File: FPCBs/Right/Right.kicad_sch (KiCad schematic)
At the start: 25 parts, among them J1 PCB, J2 LEDs, J3 LEDs, J4 shutter+1st_dial, J5 2nd Focus+Shutter, J6 Conn_01x03_Pin, SW1 Mode Dial, SW2 ON/OFF, SW3 Focus+Shutter, SW4 Focus+Shutter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

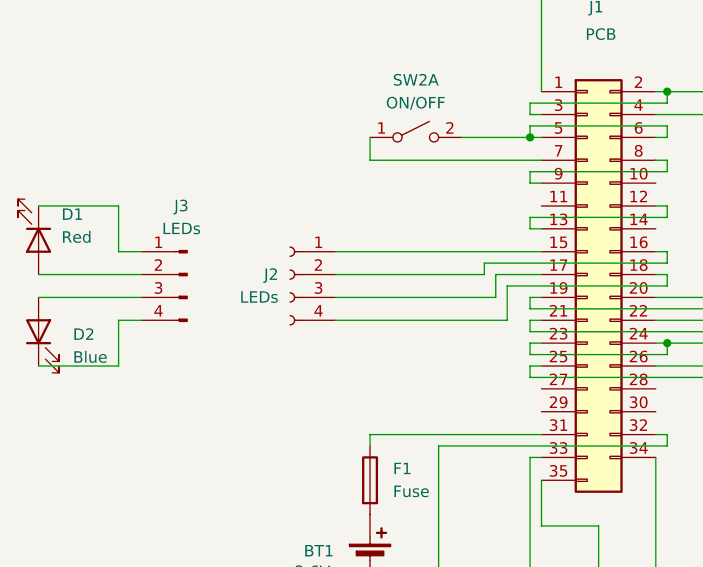
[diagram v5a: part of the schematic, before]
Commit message: Move leds to Right board
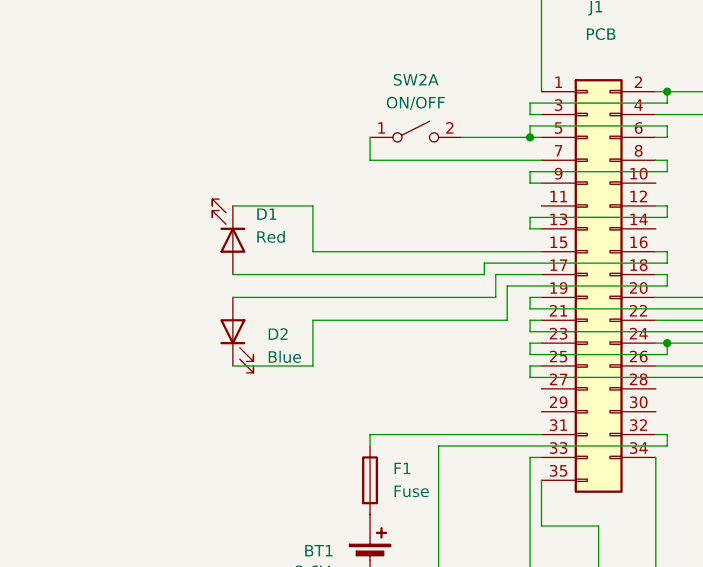
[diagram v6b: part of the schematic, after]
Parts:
- removed J2: LEDs, Leica-G9ii:Connector-4Pins, symbol Connector:Conn_01x04_Socket
- removed J3: LEDs, Leica-G9ii:Connector-4Pins, symbol Connector:Conn_01x04_Pin
- D1, D2: footprint LED_SMD:LED_0402_1005Metric -> Leica-G9ii:LED
- F1: footprint Fuse:Fuse_0402_1005Metric -> Leica-G9ii:R_2x1mm
- R1, R2, R3, R4, R5, R6, R7, R8: footprint Resistor_SMD:R_0201_0603Metric -> Leica-G9ii:R_2x1mm
- SW2: footprint Leica-G9ii:Switch_Power -> Leica-G9ii:Switch_Detection_Bidirectional
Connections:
- net at J1.15 (Pin_15): now also D1.1 (K)
- net at J1.16 (Pin_16): now also D1.2 (A)
- net at J1.17 (Pin_17): now also D2.2 (A)
- net at J1.18 (Pin_18): now also D2.1 (K)
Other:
- moved on the sheet: D1, D2
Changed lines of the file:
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@@
 	(wire
 		(pts
-			(xy 24.13 80.01) (xy 35.56 80.01)
+			(xy 45.72 80.01) (xy 74.93 80.01)
 		)
 		(stroke
@@
 	(wire
 		(pts
-			(xy 33.02 82.55) (xy 35.56 82.55)
+			(xy 54.61 82.55) (xy 76.2 82.55)
 		)
 		(stroke
@@
 	(wire
 		(pts
-			(xy 57.15 74.93) (xy 80.01 74.93)
-		)
-		(stroke
-			(width 0)
-			(type default)
-		)
-	)
-	(wire
-		(pts
 			(xy 74.93 80.01) (xy 74.93 77.47)
 		)
@@
 	(wire
 		(pts
-			(xy 57.15 82.55) (xy 76.2 82.55)
-		)
-		(stroke
-			(width 0)
-			(type default)
-		)
-	)
-	(wire
-		(pts
 			(xy 153.67 127) (xy 153.67 139.7)
 		)
@@
 	(wire
 		(pts
-			(xy 57.15 80.01) (xy 74.93 80.01)
-		)
-		(stroke
-			(width 0)
-			(type default)
-		)
-	)
-	(wire
-		(pts
 			(xy 78.74 86.36) (xy 78.74 85.09)
 		)
@@
 	(wire
 		(pts
-			(xy 24.13 69.85) (xy 33.02 69.85)
+			(xy 45.72 69.85) (xy 54.61 69.85)
 		)
 		(stroke
@@
 	(wire
 		(pts
-			(xy 33.02 87.63) (xy 33.02 82.55)
+			(xy 54.61 87.63) (xy 54.61 82.55)
 		)
 		(stroke
@@
 	(wire
 		(pts
-			(xy 57.15 77.47) (xy 73.66 77.47)
-		)
-		(stroke
-			(width 0)
-			(type default)
-		)
-	)
-	(wire
-		(pts
 			(xy 147.32 105.41) (xy 153.67 105.41)
 		)
@@
 	(wire
 		(pts
-			(xy 24.13 77.47) (xy 35.56 77.47)
+			(xy 45.72 77.47) (xy 73.66 77.47)
 		)
 		(stroke
@@
 	(wire
 		(pts
-			(xy 33.02 74.93) (xy 35.56 74.93)
+			(xy 54.61 74.93) (xy 80.01 74.93)
 		)
 		(stroke
@@
 	(wire
 		(pts
-			(xy 33.02 69.85) (xy 33.02 74.93)
+			(xy 54.61 69.85) (xy 54.61 74.93)
 		)
 		(stroke
@@
 	(wire
 		(pts
-			(xy 24.13 87.63) (xy 33.02 87.63)
+			(xy 45.72 87.63) (xy 54.61 87.63)
 		)
 		(stroke
@@
 			)
 		)
-		(property "Footprint" "Resistor_SMD:R_0201_0603Metric"
+		(property "Footprint" "Leica-G9ii:R_2x1mm"
 			(at 195.072 88.9 90)
 			(effects
@@
 	(symbol
 		(lib_id "Device:LED")
-		(at 24.13 83.82 90)
+		(at 45.72 83.82 90)
 		(unit 1)
 		(exclude_from_sim no)
@@
 		(fields_autoplaced yes)
 		(property "Reference" "D2"
-			(at 27.94 84.1374 90)
+			(at 49.53 84.1374 90)
 			(effects
 				(font
@@
 		)
 		(property "Value" "Blue"
-			(at 27.94 86.6774 90)
+			(at 49.53 86.6774 90)
 			(effects
 				(font
@@
 			)
 		)
-		(property "Footprint" "LED_SMD:LED_0402_1005Metric"
-			(at 24.13 83.82 0)
+		(property "Footprint" "Leica-G9ii:LED"
+			(at 45.72 83.82 0)
 			(effects
 				(font
@@
 		)
 		(property "Datasheet" "~"
-			(at 24.13 83.82 0)
+			(at 45.72 83.82 0)
 			(effects
 				(font
@@
 		)
 		(property "Description" "Light emitting diode"
-			(at 24.13 83.82 0)
+			(at 45.72 83.82 0)
 			(effects
 				(font
@@
 			)
 		)
-		(property "Footprint" "Resistor_SMD:R_0201_0603Metric"
+		(property "Footprint" "Leica-G9ii:R_2x1mm"
 			(at 195.072 53.34 90)
 			(effects
@@
 	(symbol
 		(lib_id "Device:LED")
-		(at 24.13 73.66 270)
+		(at 45.72 73.66 270)
 		(unit 1)
 		(exclude_from_sim no)
@@
 		(fields_autoplaced yes)
 		(property "Reference" "D1"
-			(at 26.67 70.8024 90)
+			(at 48.26 70.8024 90)
 			(effects
 				(font
@@
 		)
 		(property "Value" "Red"
-			(at 26.67 73.3424 90)
+			(at 48.26 73.3424 90)
 			(effects
 				(font
@@
 			)
 		)
-		(property "Footprint" "LED_SMD:LED_0402_1005Metric"
-			(at 24.13 73.66 0)
+		(property "Footprint" "Leica-G9ii:LED"
+			(at 45.72 73.66 0)
 			(effects
 				(font
@@
 		)
 		(property "Datasheet" "~"
-			(at 24.13 73.66 0)
+			(at 45.72 73.66 0)
 			(effects
 				(font
@@
 		)
 		(property "Description" "Light emitting diode"
-			(at 24.13 73.66 0)
+			(at 45.72 73.66 0)
 			(effects
 				(font
@@
 			)
 		)
-		(property "Footprint" "Resistor_SMD:R_0201_0603Metric"
+		(property "Footprint" "Leica-G9ii:R_2x1mm"
 			(at 195.072 73.66 90)
 			(effects
@@
 			)
 		)
-		(property "Footprint" "Resistor_SMD:R_0201_0603Metric"
+		(property "Footprint" "Leica-G9ii:R_2x1mm"
 			(at 195.072 45.72 90)
 			(effects
@@
 			)
 		)
-		(property "Footprint" "Resistor_SMD:R_0201_0603Metric"
+		(property "Footprint" "Leica-G9ii:R_2x1mm"
 			(at 195.072 81.28 90)
 			(effects
@@
 			)
 		)
-		(property "Footprint" "Resistor_SMD:R_0201_0603Metric"
+		(property "Footprint" "Leica-G9ii:R_2x1mm"
 			(at 195.072 30.48 90)
 			(effects
@@
 				(path "/4f08b7d7-0978-402f-8bca-f87716f6be32"
 					(reference "R1")
-					(unit 1)
-				)
-			)
-		)
-	)
-	(symbol
-		(lib_id "Connector:Conn_01x04_Socket")
-		(at 52.07 77.47 0)
-		(mirror y)
-		(unit 1)
-		(exclude_from_sim no)
-		(in_bom yes)
-		(on_board yes)
-		(dnp no)
-		(property "Reference" "J2"
-			(at 50.8 77.4699 0)
-			(effects
-				(font
-					(size 1.27 1.27)
-				)
-				(justify left)
-			)
-		)
-		(property "Value" "LEDs"
-			(at 50.8 80.0099 0)
-			(effects
-				(font
-					(size 1.27 1.27)
-				)
-				(justify left)
-			)
-		)
-		(property "Footprint" "Leica-G9ii:Connector-4Pins"
-			(at 52.07 77.47 0)
-			(effects
-				(font
-					(size 1.27 1.27)
-				)
-				(hide yes)
-			)
-		)
-		(property "Datasheet" "~"
-			(at 52.07 77.47 0)
-			(effects
-				(font
-					(size 1.27 1.27)
-				)
-				(hide yes)
-			)
-		)
-		(property "Description" "Generic connector, single row, 01x04, script generated"
-			(at 52.07 77.47 0)
-			(effects
-				(font
-					(size 1.27 1.27)
-				)
-				(hide yes)
-			)
-		)
-		(pin "3"
-		)
-		(pin "2"
-		)
-		(pin "1"
-		)
-		(pin "4"
-		)
-		(instances
-			(project ""
-				(path "/4f08b7d7-0978-402f-8bca-f87716f6be32"
-					(reference "J2")
 					(unit 1)
 				)
@@
 				(path "/4f08b7d7-0978-402f-8bca-f87716f6be32"
 					(reference "RV1")
-					(unit 1)
-				)
-			)
-		)
-	)
-	(symbol
-		(lib_id "Connector:Conn_01x04_Pin")
-		(at 40.64 77.47 0)
-		(mirror y)
-		(unit 1)
-		(exclude_from_sim no)
-		(in_bom yes)
-		(on_board yes)
-		(dnp no)
-		(property "Reference" "J3"
-			(at 40.005 69.85 0)
-			(effects
-				(font
-					(size 1.27 1.27)
-				)
-			)
-		)
-		(property "Value" "LEDs"
-			(at 40.005 72.39 0)
-			(effects
-				(font
-					(size 1.27 1.27)
-				)
-			)
-		)
-		(property "Footprint" "Leica-G9ii:Connector-4Pins"
-			(at 40.64 77.47 0)
-			(effects
-				(font
-					(size 1.27 1.27)
-				)
-				(hide yes)
-			)
-		)
-		(property "Datasheet" "~"
-			(at 40.64 77.47 0)
-			(effects
-				(font
-					(size 1.27 1.27)
-				)
-				(hide yes)
-			)
-		)
-		(property "Description" "Generic connector, single row, 01x04, script generated"
-			(at 40.64 77.47 0)
-			(effects
-				(font
-					(size 1.27 1.27)
-				)
-				(hide yes)
-			)
-		)
-		(pin "4"
-		)
-		(pin "2"
-		)
-		(pin "1"
-		)
-		(pin "3"
-		)
-		(instances
-			(project ""
-				(path "/4f08b7d7-0978-402f-8bca-f87716f6be32"
-					(reference "J3")
 					(unit 1)
 				)
@@
 			)
 		)
-		(property "Footprint" "Resistor_SMD:R_0201_0603Metric"
+		(property "Footprint" "Leica-G9ii:R_2x1mm"
 			(at 195.072 66.04 90)
 			(effects
@@
 			)
 		)
-		(property "Footprint" "Leica-G9ii:Switch_Power"
+		(property "Footprint" "Leica-G9ii:Switch_Detection_Bidirectional"
 			(at 66.04 62.23 0)
 			(effects
@@
 			)
 		)
-		(property "Footprint" "Resistor_SMD:R_0201_0603Metric"
+		(property "Footprint" "Leica-G9ii:R_2x1mm"
 			(at 195.072 38.1 90)
 			(effects
@@
 			)
 		)
-		(property "Footprint" "Fuse:Fuse_0402_1005Metric"
+		(property "Footprint" "Leica-G9ii:R_2x1mm"
 			(at 59.182 100.33 90)
 			(effects

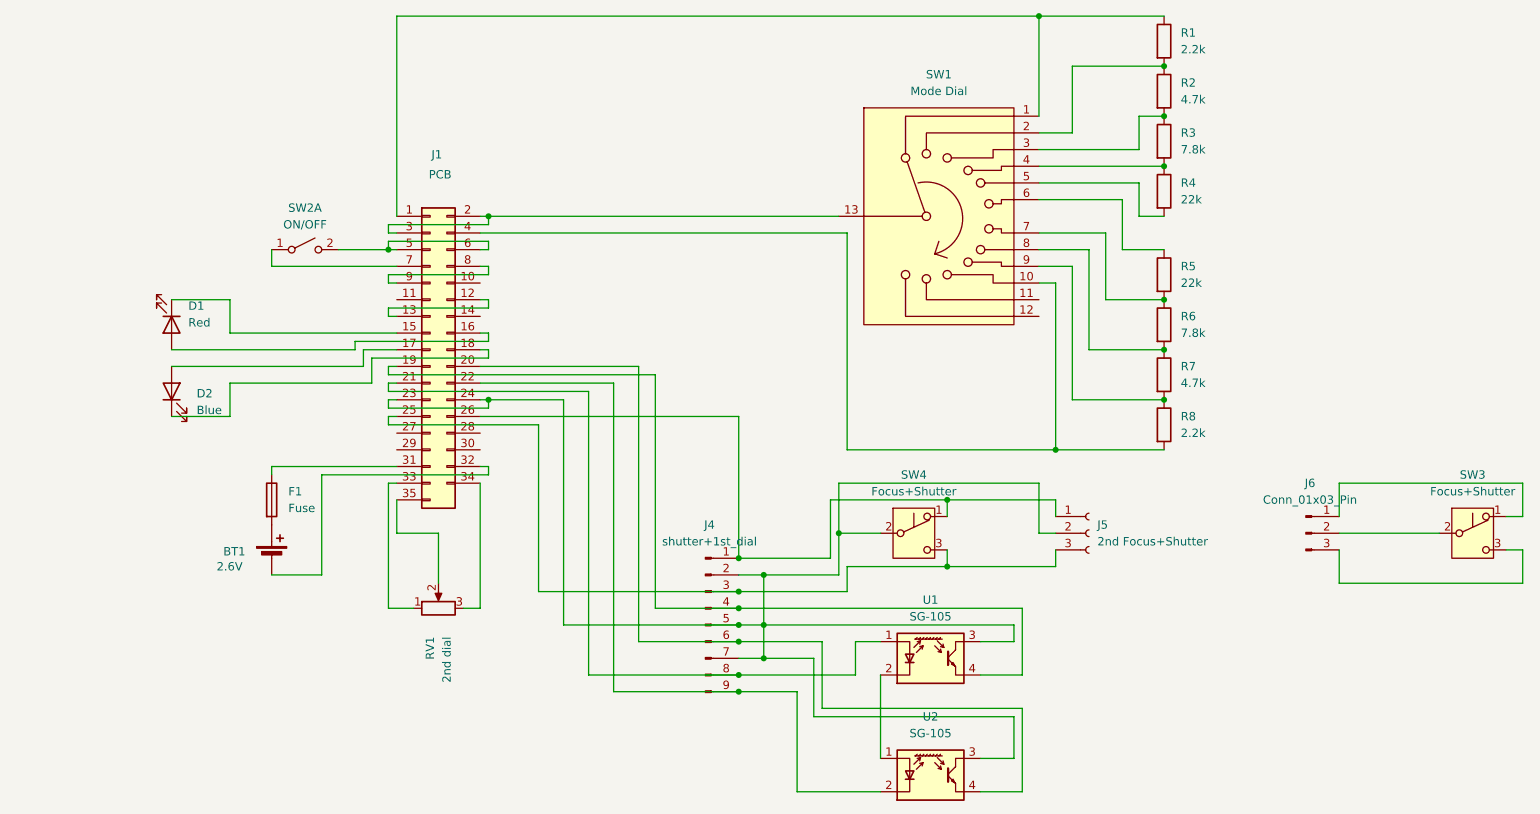
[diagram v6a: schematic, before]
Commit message: Add extra switch for on/off
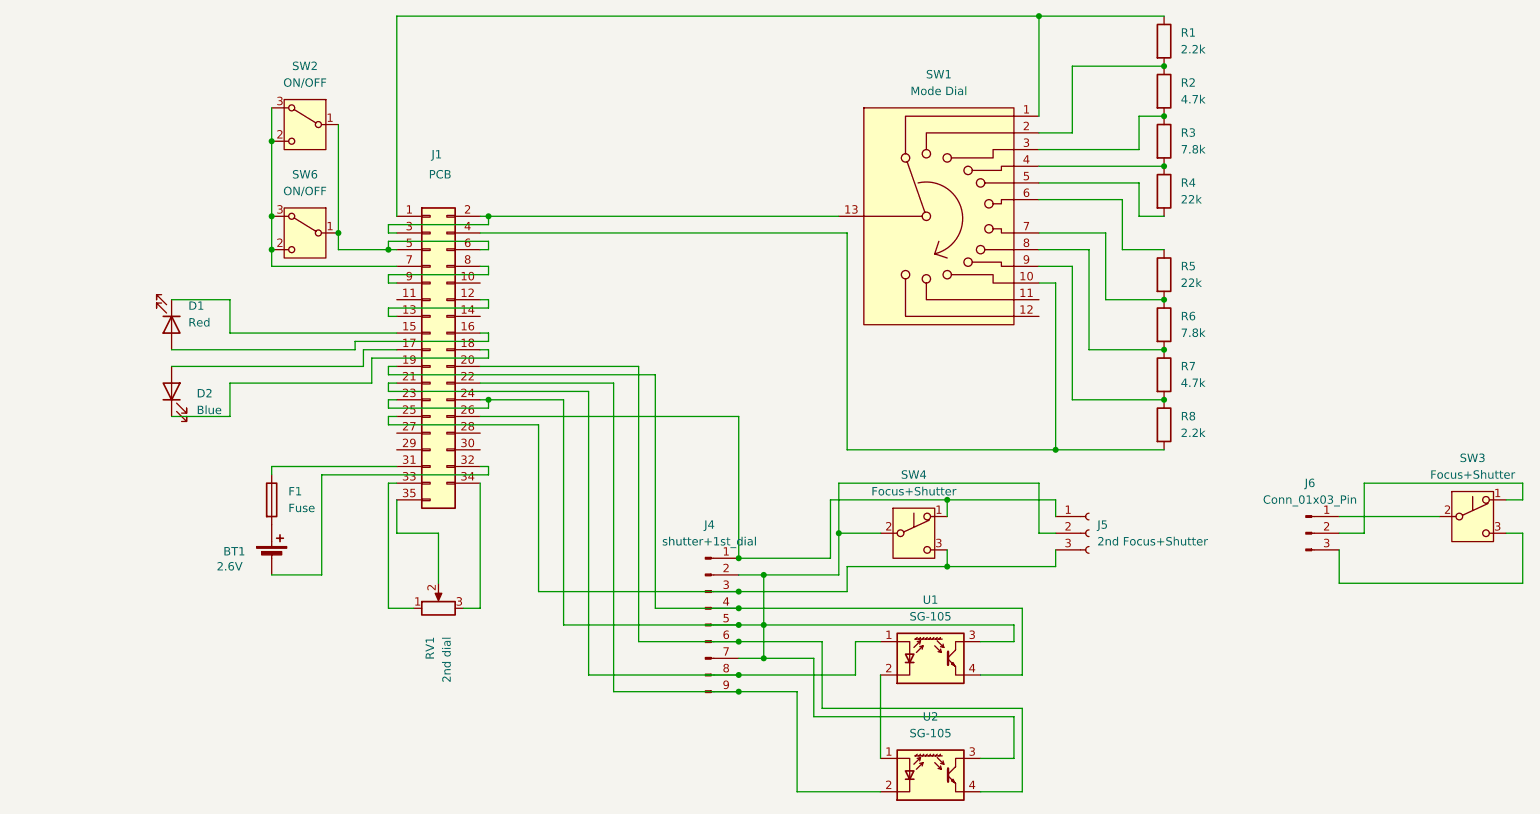
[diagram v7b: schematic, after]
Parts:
- removed SW2: ON/OFF, Leica-G9ii:Switch_Detection_Bidirectional, symbol Switch:SW_DPST_x2
- added SW2, SW6: ON/OFF, Leica-G9ii:Switch_Detection_Bidirectional, symbol Switch:SW_SPDT_312
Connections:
- net at J1.5 (Pin_5), J1.6 (Pin_6): now also SW2.1 (B), SW6.1 (B)
- net at J1.7 (Pin_7): now also SW2.2 (C), SW2.3 (A), SW6.2 (C), SW6.3 (A)
- net at SW3.1 (A): now also J6.2 (Pin_2); no longer J6.1 (Pin_1)
- net at SW3.2 (B): now also J6.1 (Pin_1); no longer J6.2 (Pin_2)
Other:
- moved on the sheet: SW3
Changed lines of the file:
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@@
 	)
 	(junction
+		(at 60.96 62.23)
+		(diameter 0)
+		(color 0 0 0 0)
+	)
+	(junction
+		(at 60.96 57.15)
+		(diameter 0)
+		(color 0 0 0 0)
+	)
+	(junction
 		(at 196.85 69.85)
 		(diameter 0)
@@
 	)
 	(junction
+		(at 60.96 45.72)
+		(diameter 0)
+		(color 0 0 0 0)
+	)
+	(junction
 		(at 147.32 105.41)
 		(diameter 0)
@@
 	)
 	(junction
+		(at 71.12 59.69)
+		(diameter 0)
+		(color 0 0 0 0)
+	)
+	(junction
 		(at 180.34 92.71)
 		(diameter 0)
@@
 	(wire
 		(pts
-			(xy 251.46 107.95) (xy 248.92 107.95)
+			(xy 251.46 105.41) (xy 248.92 105.41)
 		)
 		(stroke
@@
 	(wire
 		(pts
+			(xy 227.33 105.41) (xy 223.52 105.41)
+		)
+		(stroke
+			(width 0)
+			(type default)
+		)
+	)
+	(wire
+		(pts
 			(xy 73.66 76.2) (xy 93.98 76.2)
 		)
@@
 	(wire
 		(pts
+			(xy 60.96 57.15) (xy 60.96 62.23)
+		)
+		(stroke
+			(width 0)
+			(type default)
+		)
+	)
+	(wire
+		(pts
 			(xy 180.34 67.31) (xy 180.34 92.71)
 		)
@@
 	(wire
 		(pts
+			(xy 60.96 45.72) (xy 60.96 57.15)
+		)
+		(stroke
+			(width 0)
+			(type default)
+		)
+	)
+	(wire
+		(pts
 			(xy 54.61 82.55) (xy 76.2 82.55)
 		)
@@
 	(wire
 		(pts
-			(xy 223.52 105.41) (xy 238.76 105.41)
+			(xy 78.74 88.9) (xy 101.6 88.9)
 		)
 		(stroke
@@
 	(wire
 		(pts
-			(xy 78.74 88.9) (xy 101.6 88.9)
+			(xy 86.36 113.03) (xy 86.36 105.41)
 		)
 		(stroke
@@
 	(wire
 		(pts
-			(xy 86.36 113.03) (xy 86.36 105.41)
+			(xy 71.12 59.69) (xy 71.12 62.23)
 		)
 		(stroke
@@
 	(wire
 		(pts
-			(xy 251.46 113.03) (xy 251.46 107.95)
+			(xy 251.46 113.03) (xy 251.46 105.41)
 		)
 		(stroke
@@
 	(wire
 		(pts
-			(xy 251.46 102.87) (xy 251.46 97.79)
+			(xy 251.46 100.33) (xy 251.46 97.79)
+		)
+		(stroke
+			(width 0)
+			(type default)
+		)
+	)
+	(wire
+		(pts
+			(xy 71.12 43.18) (xy 71.12 59.69)
 		)
 		(stroke
@@
 	(wire
 		(pts
-			(xy 78.74 86.36) (xy 78.74 85.09)
+			(xy 60.96 40.64) (xy 60.96 45.72)
 		)
 		(stroke
@@
 	(wire
 		(pts
-			(xy 223.52 97.79) (xy 223.52 102.87)
+			(xy 78.74 86.36) (xy 78.74 85.09)
 		)
 		(stroke
@@
 	(wire
 		(pts
-			(xy 251.46 97.79) (xy 223.52 97.79)
+			(xy 251.46 97.79) (xy 227.33 97.79)
 		)
 		(stroke
@@
 	(wire
 		(pts
-			(xy 248.92 102.87) (xy 251.46 102.87)
+			(xy 248.92 100.33) (xy 251.46 100.33)
 		)
 		(stroke
@@
 	(wire
 		(pts
+			(xy 227.33 97.79) (xy 227.33 105.41)
+		)
+		(stroke
+			(width 0)
+			(type default)
+		)
+	)
+	(wire
+		(pts
 			(xy 93.98 64.77) (xy 93.98 66.04)
 		)
@@
 	(wire
 		(pts
+			(xy 223.52 102.87) (xy 238.76 102.87)
+		)
+		(stroke
+			(width 0)
+			(type default)
+		)
+	)
+	(wire
+		(pts
 			(xy 80.01 100.33) (xy 80.01 105.41)
 		)
@@
 	(symbol
 		(lib_id "Switch:SW_Push_SPDT")
-		(at 243.84 105.41 0)
+		(at 243.84 102.87 0)
 		(unit 1)
 		(exclude_from_sim no)
@@
 		(fields_autoplaced yes)
 		(property "Reference" "SW3"
-			(at 243.84 96.52 0)
+			(at 243.84 93.98 0)
 			(effects
 				(font
@@
 		)
 		(property "Value" "Focus+Shutter"
-			(at 243.84 99.06 0)
+			(at 243.84 96.52 0)
 			(effects
 				(font
@@
 		)
 		(property "Footprint" "Leica-G9ii:Switch_Shutter_1"
-			(at 243.84 105.41 0)
+			(at 243.84 102.87 0)
 			(effects
 				(font
@@
 		)
 		(property "Datasheet" "~"
-			(at 243.84 105.41 0)
+			(at 243.84 102.87 0)
 			(effects
 				(font
@@
 		)
 		(property "Description" "Momentary Switch, single pole double throw"
-			(at 243.84 105.41 0)
+			(at 243.84 102.87 0)
 			(effects
 				(font
@@
 	)
 	(symbol
-		(lib_id "Switch:SW_DPST_x2")
-		(at 66.04 62.23 0)
+		(lib_id "Device:R")
+		(at 196.85 38.1 0)
 		(unit 1)
 		(exclude_from_sim no)
@@
 		(dnp no)
 		(fields_autoplaced yes)
-		(property "Reference" "SW2"
-			(at 66.04 55.88 0)
+		(property "Reference" "R2"
+			(at 199.39 36.8299 0)
 			(effects
 				(font
 					(size 1.27 1.27)
 				)
+				(justify left)
 			)
 		)
-		(property "Value" "ON/OFF"
-			(at 66.04 58.42 0)
+		(property "Value" "4.7k"
+			(at 199.39 39.3699 0)
 			(effects
 				(font
 					(size 1.27 1.27)
 				)
+				(justify left)
 			)
 		)
-		(property "Footprint" "Leica-G9ii:Switch_Detection_Bidirectional"
-			(at 66.04 62.23 0)
+		(property "Footprint" "Leica-G9ii:R_2x1mm"
+			(at 195.072 38.1 90)
 			(effects
 				(font
@@
 		)
 		(property "Datasheet" "~"
-			(at 66.04 62.23 0)
+			(at 196.85 38.1 0)
 			(effects
 				(font
@@
 			)
 		)
-		(property "Description" "Single Pole Single Throw (SPST) switch, separate symbol"
-			(at 66.04 62.23 0)
+		(property "Description" "Resistor"
+			(at 196.85 38.1 0)
 			(effects
 				(font
@@
 			)
 		)
-		(pin "1"
-		)
 		(pin "2"
 		)
-		(pin "3"
-		)
-		(pin "4"
+		(pin "1"
 		)
 		(instances
 			(project ""
 				(path "/4f08b7d7-0978-402f-8bca-f87716f6be32"
-					(reference "SW2")
+					(reference "R2")
 					(unit 1)
 				)
@@
 	)
 	(symbol
-		(lib_id "Device:R")
-		(at 196.85 38.1 0)
+		(lib_id "Switch:SW_SPDT_312")
+		(at 66.04 43.18 0)
+		(mirror y)
 		(unit 1)
 		(exclude_from_sim no)
@@
 		(dnp no)
 		(fields_autoplaced yes)
-		(property "Reference" "R2"
-			(at 199.39 36.8299 0)
+		(property "Reference" "SW2"
+			(at 66.04 34.29 0)
 			(effects
 				(font
 					(size 1.27 1.27)
 				)
-				(justify left)
 			)
 		)
-		(property "Value" "4.7k"
-			(at 199.39 39.3699 0)
+		(property "Value" "ON/OFF"
+			(at 66.04 36.83 0)
 			(effects
 				(font
 					(size 1.27 1.27)
 				)
-				(justify left)
 			)
 		)
-		(property "Footprint" "Leica-G9ii:R_2x1mm"
-			(at 195.072 38.1 90)
+		(property "Footprint" "Leica-G9ii:Switch_Detection_Bidirectional"
+			(at 66.04 53.34 0)
 			(effects
 				(font
@@
 		)
 		(property "Datasheet" "~"
-			(at 196.85 38.1 0)
+			(at 66.04 50.8 0)
 			(effects
 				(font
@@
 			)
 		)
-		(property "Description" "Resistor"
-			(at 196.85 38.1 0)
+		(property "Description" "Switch, single pole double throw"
+			(at 66.04 43.18 0)
 			(effects
 				(font
@@
 			)
 		)
+		(pin "3"
+		)
 		(pin "2"
 		)
@@
 		)
 		(instances
-			(project ""
+			(project "Right"
 				(path "/4f08b7d7-0978-402f-8bca-f87716f6be32"
-					(reference "R2")
+					(reference "SW2")
 					(unit 1)
 				)
@@
 					(unit 1)
 				)
+			)
+		)
+	)
+	(symbol
+		(lib_id "Switch:SW_SPDT_312")
+		(at 66.04 59.69 0)
+		(mirror y)
+		(unit 1)
+		(exclude_from_sim no)
+		(in_bom yes)
+		(on_board yes)
+		(dnp no)
+		(fields_autoplaced yes)
+		(property "Reference" "SW6"
+			(at 66.04 50.8 0)
+			(effects
+				(font
+					(size 1.27 1.27)
+				)
+			)
+		)
+		(property "Value" "ON/OFF"
+			(at 66.04 53.34 0)
+			(effects
+				(font
+					(size 1.27 1.27)
+				)
+			)
+		)
+		(property "Footprint" "Leica-G9ii:Switch_Detection_Bidirectional"
+			(at 66.04 69.85 0)
+			(effects
+				(font
+					(size 1.27 1.27)
+				)
+				(hide yes)
+			)
+		)
+		(property "Datasheet" "~"
+			(at 66.04 67.31 0)
+			(effects
+				(font
+					(size 1.27 1.27)
+				)
+				(hide yes)
+			)
+		)
+		(property "Description" "Switch, single pole double throw"
+			(at 66.04 59.69 0)
+			(effects
+				(font
+					(size 1.27 1.27)
+				)
+				(hide yes)
+			)
+		)
+		(pin "3"
+		)
+		(pin "2"
+		)
+		(pin "1"
+		)
+		(instances
+			(project ""
+				(path "/4f08b7d7-0978-402f-8bca-f87716f6be32"
+					(reference "SW6")
+					(unit 1)
+				)
